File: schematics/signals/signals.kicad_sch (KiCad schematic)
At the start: 30 parts, among them J1 Conditioned, J2 Sensors, U1 INA849D, U2 OPA2182, U3 INA849D

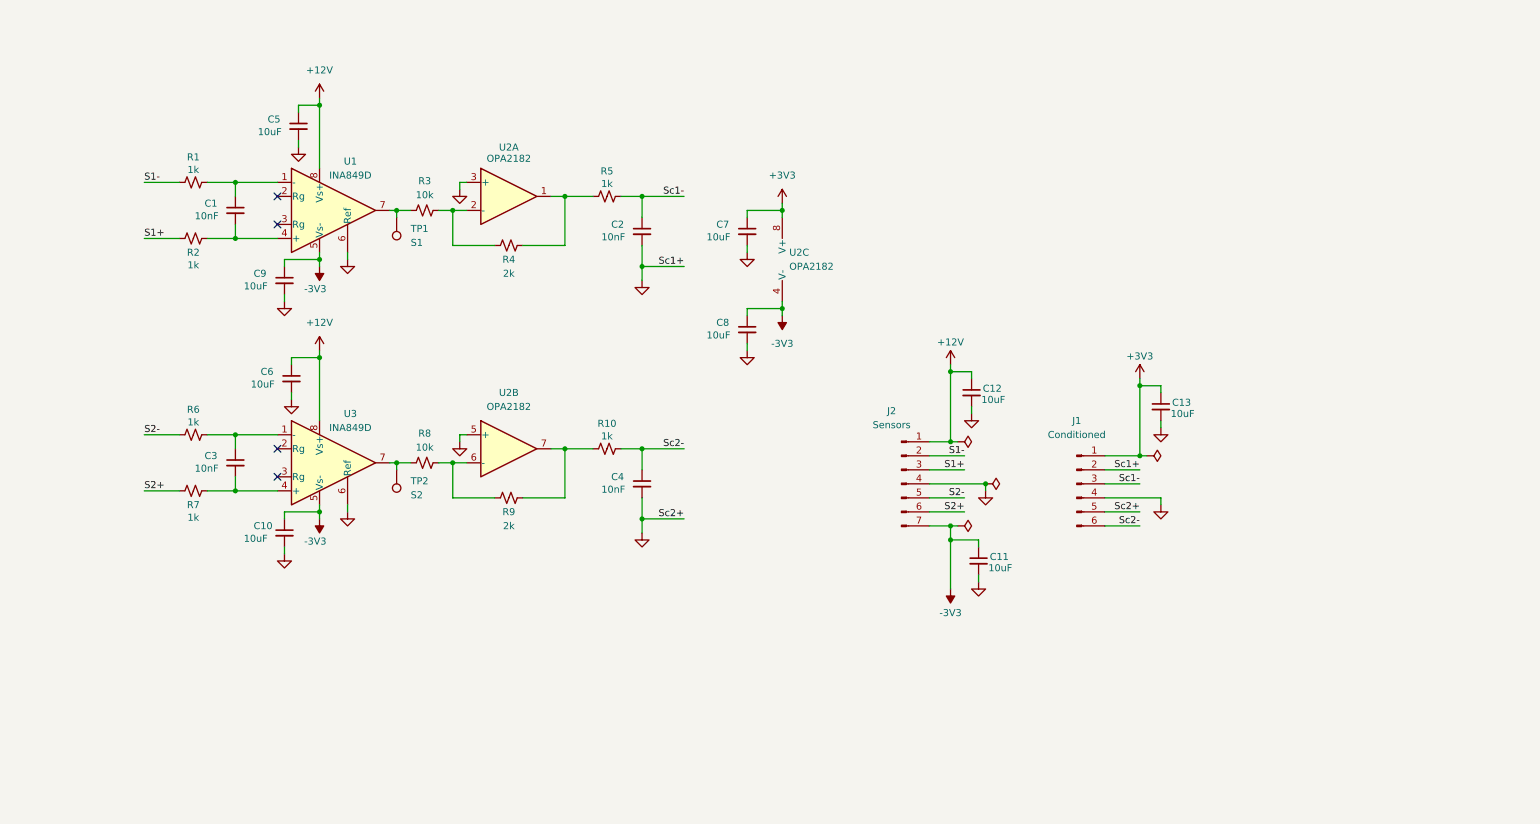
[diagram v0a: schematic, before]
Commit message: update(signals): review
1. Add notes to schematics
2. Switch out INA849 for AD8422ARMZ to help with input bias current
3. Add open R_g pads to AD8422
4. Add dip switches for R_f in OPA circuit
5. Fix pinout
	Initial abalmos and I discussed switching the pinout so the
	input to the ADC was the correct direction and the inversion was
	at the inputs to the INA. This cannot work due to the
	asymmetrical supplies

TODO:
1. Update motherboard
2. Add MFB bessel filter
3. Make slightly bigger in case of later revisions (optional)
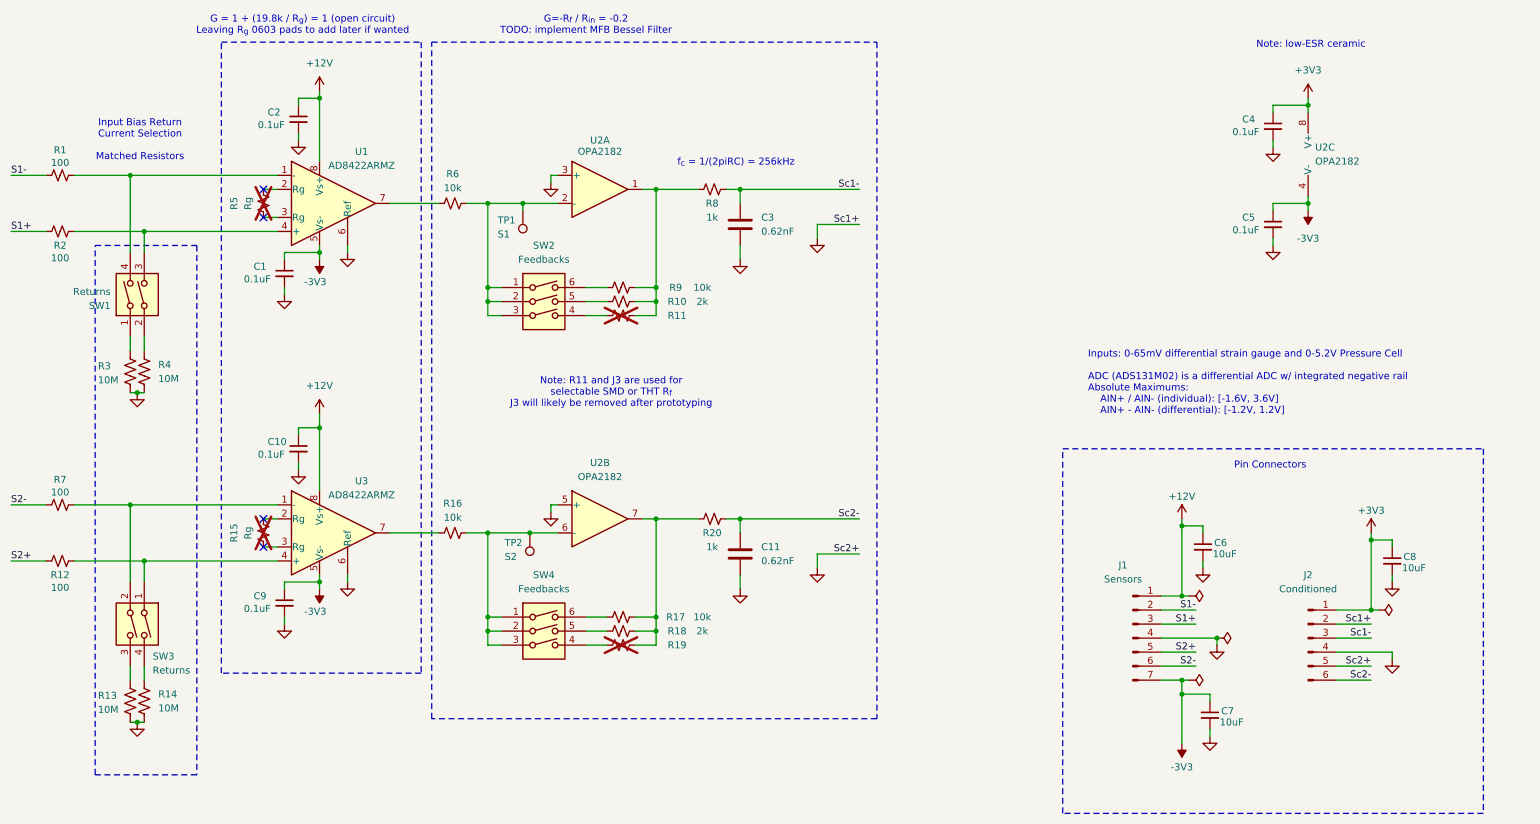
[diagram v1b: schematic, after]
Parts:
- removed C1, C2, C3, C4: 10nF, Capacitor_SMD:C_0603_1608Metric, symbol Device:C_Small
- removed C6: 10uF, Capacitor_SMD:C_0603_1608Metric, symbol Device:C_Small
- removed R4: 2k, Resistor_SMD:R_0603_1608Metric, symbol Device:R_Small_US
- removed R6: 1k, Resistor_SMD:R_0603_1608Metric, symbol Device:R_Small_US
- removed U1, U3: INA849D, Package_SO:SOIC-8_3.9x4.9mm_P1.27mm, symbol Amplifier_Instrumentation:INA849D
- added C11, C3: 0.62nF, Capacitor_SMD:C_0603_1608Metric, symbol Device:C
- added C9: 0.1uF, Capacitor_SMD:C_0603_1608Metric, symbol Device:C_Small
- added R11, R18, R19: 2k, Resistor_SMD:R_0603_1608Metric, symbol Device:R_Small_US
- added R12: 100, Resistor_SMD:R_0603_1608Metric, symbol Device:R_Small_US
- added R13, R14, R3, R4: 10M, Resistor_SMD:R_0603_1608Metric, symbol Device:R_US
- added R15: Rg, Resistor_SMD:R_0603_1608Metric, symbol Device:R_Small_US
- added R16, R17: 10k, Resistor_SMD:R_0603_1608Metric, symbol Device:R_Small_US
- added R20: 1k, Resistor_SMD:R_0603_1608Metric, symbol Device:R_Small_US
- added SW1, SW3: Returns, Button_Switch_SMD:SW_DIP_SPSTx02_Slide_KingTek_DSHP02TJ_W5.25mm_P1.27mm_JPin, symbol Switch:SW_DIP_x02
- added SW2, SW4: Feedbacks, Button_Switch_SMD:SW_DIP_SPSTx03_Slide_KingTek_DSHP03TJ_W5.25mm_P1.27mm_JPin, symbol Switch:SW_DIP_x03
- added U1, U3: AD8422ARMZ, Package_SO:SOIC-8_3.9x4.9mm_P1.27mm, symbol Amplifier_Instrumentation:AD8422ARMZ
- C1: renamed from C9; value 10uF -> 0.1uF
- C10: value 10uF -> 0.1uF
- C2: renamed from C5; value 10uF -> 0.1uF
- C4: renamed from C7; value 10uF -> 0.1uF
- C5: renamed from C8; value 10uF -> 0.1uF
- R1, R2, R7: value 1k -> 100
- R10: value 1k -> 2k
- R5: value 1k -> Rg; now not fitted
- R8: value 10k -> 1k
- R9: value 2k -> 10k
- renumbered C12 to C6, C11 to C7, C13 to C8, J2 to J1, J1 to J2, R3 to R6
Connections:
- net +12V: now also C10.1, U1.8 (Vs+), U3.8 (Vs+)
- net -3V3: now also C9.1, U1.5 (Vs-), U3.5 (Vs-); no longer C10.1
- net GND: now also C11.2, C3.2, C9.2, R13.2, R14.2, R3.2, R4.2, U1.6 (Ref), U3.6 (Ref)
- net S2+: now also J1.5 (Pin_5), R12.1; no longer J1.6 (Pin_6), R7.1
- net S2-: now also J1.6 (Pin_6), R7.1; no longer J1.5 (Pin_5)
- net Sc1-: now also R8.2, C3.1; no longer R5.2
- net Sc2-: now also C11.1, R20.2; no longer R10.2
- net at R6.2, U2.2 (-): now also TP1.1, SW2.1, SW2.2, SW2.3
- net at R5.1: now also U1.3 (Rg); no longer U2.1
- net at R7.2: now also SW3.2, U3.1 (-)
- net at R1.2: now also SW1.4, U1.1 (-)
- net at R2.2: now also SW1.3, U1.4 (+)
- net at R6.1: now also U1.7; no longer TP1.1
- net at TP2.1: now also U2.6 (-), R16.2, SW4.1, SW4.2, SW4.3; no longer R8.1
- new net: R18.1, SW4.5
- new net: R17.2, R18.2, R19.2, R20.1, U2.7
- new net: R3.1, SW1.1
- new net: R4.1, SW1.2
- new net: R14.1, SW3.4
- new net: R16.1, U3.7
- new net: R12.2, SW3.1, U3.4 (+)
- new net: R15.2, U3.2 (Rg)
- new net: R15.1, U3.3 (Rg)
- new net: R5.2, U1.2 (Rg)
- new net: R10.1, SW2.5
- new net: R10.2, R11.2, R8.1, R9.2, U2.1
- new net: R9.1, SW2.6
- new net: R17.1, SW4.6
- new net: R19.1, SW4.4
- new net: R13.1, SW3.3
- new net: R11.1, SW2.4
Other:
- note added: "G = 1 + (19.8k / R_{g}) = 1 (open circuit) Leaving R_{g} 0603 pads to add later if wanted"
- note added: "G=-R_{f} / R_{in} = -0.2 TODO: implement MFB Bessel Filter"
- note added: "Input Bias Return Current Selection Matched Resistors"
- note added: "Inputs: 0-65mV differential strain gauge and 0-5.2V Pressure Cell ADC (ADS131M02) is a differential ADC w/ integrated negative rail Absolute Maximums: AIN+ / AIN- (individual): [-1.6V, 3.6V] AIN+ - AIN- (differential): [-1.2V, 1.2V]"
- note added: "Note: R11 and J3 are used for selectable SMD or THT R_{f} J3 will likely be removed after prototyping"
- note added: "Note: low-ESR ceramic"
- note added: "Pin Connectors"
- note added: "f_{c} = 1/(2piRC) = 256kHz"
- moved on the sheet: C1, C2, C4, C5, C6, C7, C8, J1, J2, R1, R2, R6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

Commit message: update(motherboard): fix from signals review
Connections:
- net S1+: now also J1.2 (Pin_2); no longer J1.3 (Pin_3)
- net S1-: now also J1.3 (Pin_3); no longer J1.2 (Pin_2)
- net S2+: now also J1.6 (Pin_6); no longer J1.5 (Pin_5)
- net S2-: now also J1.5 (Pin_5); no longer J1.6 (Pin_6)
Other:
- note added: "G = 1 + (19.8k / R_{g}) = 1 (open) Leaving R_{g} 0603 pads to add later"
- note added: "Input Bias Return Current Selection"
- note removed: "G = 1 + (19.8k / R_{g}) = 1 (open circuit) Leaving R_{g} 0603 pads to add later if wanted"
- note removed: "Input Bias Return Current Selection Matched Resistors"
- moved on the sheet: C4, C5, C6, C7, C8, J1, J2, U2C

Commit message: production: exported for jlc, had to change some parts for stocking
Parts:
- C6, C7, C8: footprint Capacitor_SMD:C_0603_1608Metric -> Capacitor_SMD:C_0805_2012Metric
- U1, U3: footprint Package_SO:SOIC-8_3.9x4.9mm_P1.27mm -> Package_SO:MSOP-8_3x3mm_P0.65mm
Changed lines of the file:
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@@
 			)
 		)
-		(property "Footprint" "Capacitor_SMD:C_0603_1608Metric"
+		(property "Footprint" "Capacitor_SMD:C_0805_2012Metric"
 			(at 234.95 147.32 0)
 			(hide yes)
@@
 			)
 		)
-		(property "Footprint" "Capacitor_SMD:C_0603_1608Metric"
+		(property "Footprint" "Capacitor_SMD:C_0805_2012Metric"
 			(at 233.68 116.84 0)
 			(hide yes)
@@
 			)
 		)
-		(property "Footprint" "Package_SO:SOIC-8_3.9x4.9mm_P1.27mm"
+		(property "Footprint" "Package_SO:MSOP-8_3x3mm_P0.65mm"
 			(at 68.58 110.49 0)
 			(hide yes)
@@
 			)
 		)
-		(property "Footprint" "Package_SO:SOIC-8_3.9x4.9mm_P1.27mm"
+		(property "Footprint" "Package_SO:MSOP-8_3x3mm_P0.65mm"
 			(at 68.58 50.8 0)
 			(hide yes)
@@
 			)
 		)
-		(property "Footprint" "Capacitor_SMD:C_0603_1608Metric"
+		(property "Footprint" "Capacitor_SMD:C_0805_2012Metric"
 			(at 267.97 119.38 0)
 			(hide yes)

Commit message: release: 'LCSC Part #' and 'FT Rotation Offset'
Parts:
- C1, C10, C2, C4, C5, C9: LCSC Part # (none) -> C14663
- C11, C3: LCSC Part # (none) -> C2961268
- C6, C7, C8: LCSC Part # (none) -> C440198
- J1, J2, R15, R5, TP1, TP2: now left out of the parts list
- R1, R12, R2, R7: LCSC Part # (none) -> C122970
- R10, R18: LCSC Part # (none) -> C136954
- R11, R19: value 2k -> Rf; now left out of the parts list
- R13, R14, R3, R4: LCSC Part # (none) -> C7250
- R16, R17, R6, R9: LCSC Part # (none) -> C95204
- R20, R8: LCSC Part # (none) -> C110776
- SW1, SW3: FT Rotation Offset (none) -> 90; LCSC Part # (none) -> C3293149
- SW2, SW4: FT Rotation Offset (none) -> -90; LCSC Part # (none) -> C5123689
- U1, U3: LCSC Part # (none) -> C668395
- U2: FT Rotation Offset (none) -> -90; LCSC Part # (none) -> C2873420

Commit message: feat(signals): bessel filter
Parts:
- removed C11, C3: 0.62nF, Capacitor_SMD:C_0603_1608Metric, symbol Device:C
- removed R7: 100, Resistor_SMD:R_0603_1608Metric, symbol Device:R_Small_US
- added C11: 0.1uF, Capacitor_SMD:C_0603_1608Metric, symbol Device:C_Small
- added C12: 220pF, Capacitor_SMD:C_0603_1608Metric, symbol Device:C_Small
- added C13, C3: 100pF, Capacitor_SMD:C_0603_1608Metric, symbol Device:C_Small
- added R6: 33.2k, Resistor_SMD:R_0603_1608Metric, symbol Device:R_Small_US
- C9: value 0.1uF -> 220pF
- R10: value 2k -> 6.65k; LCSC Part # C136954 -> C95204
- R11: value Rf -> 100; LCSC Part # (none) -> C122970; now fitted; now in the parts list
- R14: LCSC Part # C7250 -> C7250
- R16: value 10k -> 33.2k
- R17, R9: value 10k -> 6.65k
- R18: value 2k -> (none); LCSC Part # C136954 -> C95204; now not fitted
- R19: value Rf -> 6.65k; LCSC Part # (none) -> C95204; now fitted; now in the parts list
- R20: value 1k -> 6.65k; LCSC Part # C110776 -> C95204
- R7: renamed from R6; value 10k -> 6.65k
- R8: value 1k -> (none); LCSC Part # C110776 -> C95204; now not fitted
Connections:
- net +12V: now also C11.1; no longer C10.1
- net -3V3: now also C10.1; no longer C9.1
- net GND: now also C9.1, C11.2, C12.1; no longer C9.2
- net S2-: now also R11.1
- net Sc1-: now also R9.2, U2.1, C3.2; no longer R8.2
- net Sc2-: now also U2.7, C13.2
- net at R18.1: now also SW4.4; no longer SW4.5
- net at R17.2, R18.2, R20.1: now also R16.2, R19.1, TP2.1, C12.2; no longer R19.2, U2.7
- net at R14.1: now also SW3.2; no longer SW3.4
- net at U3.7: now also SW4.1, SW4.2, SW4.3; no longer R16.1
- net at R12.2, U3.4 (+): now also SW3.3; no longer SW3.1
- net at U3.1 (-): now also R11.2, SW3.4; no longer SW3.2
- net at U1.7: now also SW2.1, SW2.2, SW2.3; no longer R7.1
- net at R10.1: now also C9.2, R7.2, R8.2, R9.1, TP1.1, R6.2; no longer SW2.5
- net at SW2.6: now also R6.1; no longer R9.1
- net at SW4.6: now also R16.1; no longer R17.1
- net at R13.1: now also SW3.1; no longer SW3.3
- net at SW2.4: now also R8.1; no longer R11.1
- new net: C13.1, R19.2, U2.6 (-)
- new net: C3.1, R10.2, U2.2 (-)
- new net: R7.1, SW2.5
- new net: R17.1, SW4.5
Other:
- note removed: "Note: R11 and J3 are used for selectable SMD or THT R_{f} J3 will likely be removed after prototyping"
- note removed: "f_{c} = 1/(2piRC) = 256kHz"
- moved on the sheet: R7, R9, SW2, TP1, U2A
